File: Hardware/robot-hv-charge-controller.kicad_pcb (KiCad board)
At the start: 2 copper layers, 100 x 100 mm, 136 parts, among them J1 USB2.0_16P, J2 UART_CONN, J3 XT30PW-M, J4 Conn_01x02, J5 XT60PW-M, J6 Conn_01x02, J7 XT60PW-M, J8 Conn_01x03, J9 Conn_01x02, Q2 2SD882, Q3 BC817, Q4 BC817, Q5 2SD882, Q6 2SD882, Q7 MJD41CT4G, SW1 ENABLE, U1 TCAN3414DR, U10 LTV-356T, U11 LTV-356T, U12 LTV-356T, U13 LTV-356T, U14 LTV-356T, U15 CH340C, U2 INA240A1PW, U3 MAX3485, U4 ESP32-WROOM-32E, U5 USBLC6-2SC6, U6 LTV-356T, U7 TLV1117-33, U8 HF116F-80/24-1HTF, U9 LV14340DDAR

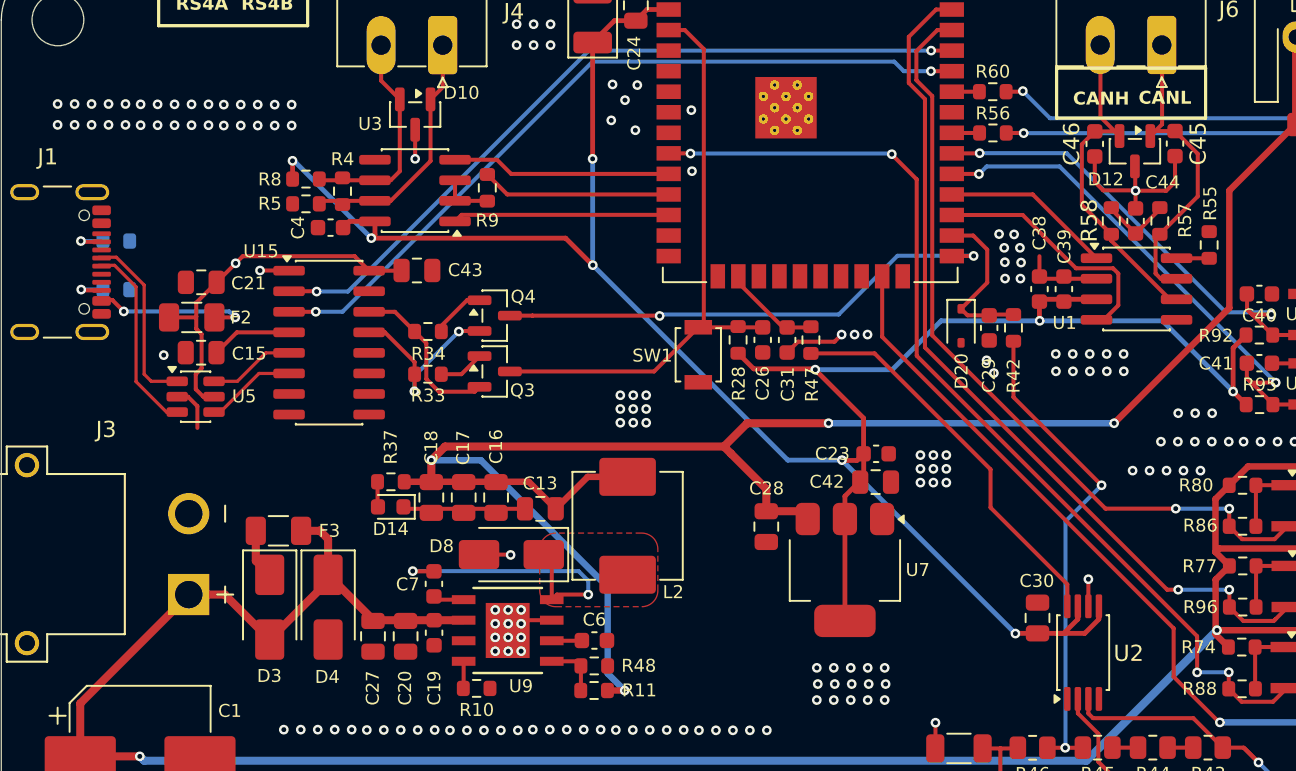
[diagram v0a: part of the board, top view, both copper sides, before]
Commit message: fix(hardware): revise optocoupler control logic
Update relay and communication optocoupler drive networks, then synchronize the related PCB routing and KiCad project metadata.
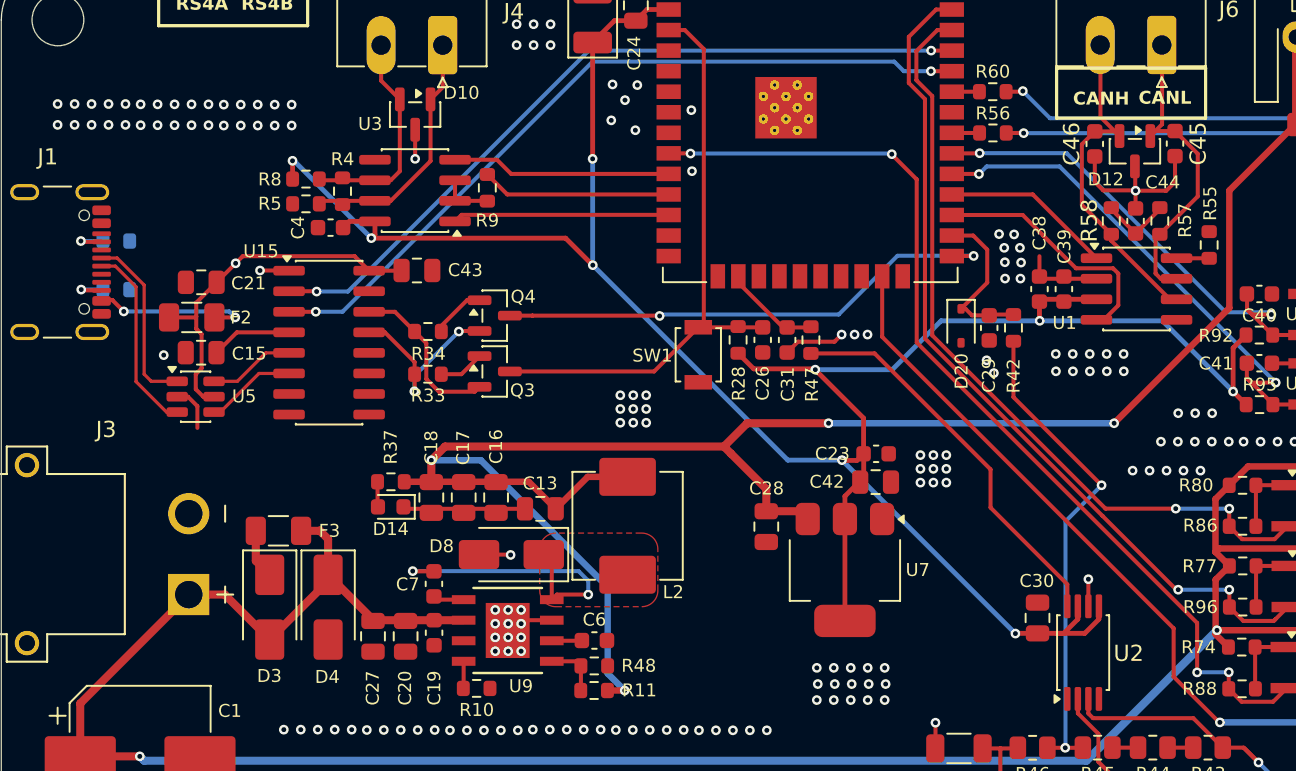
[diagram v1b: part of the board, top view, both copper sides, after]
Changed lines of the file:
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@@
 			(layer "F.Cu"
 				(type "copper")
-				(thickness 0.035)
+				(thickness 0.07)
 			)
 			(layer "dielectric 1"
 				(type "core")
-				(thickness 1.51)
+				(color "FR4 natural")
+				(thickness 1.44)
 				(material "FR4")
 				(epsilon_r 4.5)
@@
 			(layer "B.Cu"
 				(type "copper")
-				(thickness 0.035)
+				(thickness 0.07)
 			)
 			(layer "B.Mask"
@@
 		(capping no)
 		(filling no)
+		(zone_defaults)
 		(pcbplotparams
 			(layerselection 0x00000000_00000000_55555555_55555550)
@@
 	)
 	(segment
+		(start 159.6 51.36)
+		(end 159.32 51.36)
+		(width 0.25)
+		(layer "F.Cu")
+		(net "/Output_Protection_And_Sensing/VOUT_SENSE_ADC")
+	)
+	(segment
 		(start 160.94 49.74)
 		(end 160.94 47.7)
@@
 	(segment
 		(start 161.06 51.7625)
-		(end 159.7225 51.7625)
+		(end 160.0025 51.7625)
 		(width 0.25)
 		(layer "F.Cu")
@@
 	)
 	(segment
-		(start 159.7225 51.7625)
-		(end 159.32 51.36)
+		(start 160.0025 51.7625)
+		(end 159.6 51.36)
 		(width 0.25)
 		(layer "F.Cu")
@@
 	)
 	(segment
-		(start 141.25 41.75)
-		(end 142.59 41.75)
+		(start 156.58 43.36)
+		(end 156.58 53.443884)
 		(width 0.25)
 		(layer "F.Cu")
@@
 	)
 	(segment
-		(start 173.91 71.59)
-		(end 173.91 73.83)
+		(start 141.25 41.75)
+		(end 142.59 41.75)
 		(width 0.25)
 		(layer "F.Cu")
@@
 	)
 	(segment
-		(start 178.6075 75.645)
-		(end 176.665 75.645)
+		(start 173.91 70.773884)
+		(end 173.91 73.83)
 		(width 0.25)
 		(layer "F.Cu")
@@
 	)
 	(segment
-		(start 142.59 41.75)
-		(end 142.6 41.76)
+		(start 155.04 41.82)
+		(end 156.58 43.36)
 		(width 0.25)
 		(layer "F.Cu")
@@
 	)
 	(segment
-		(start 156.58 54.26)
-		(end 173.91 71.59)
+		(start 178.6075 75.645)
+		(end 176.665 75.645)
 		(width 0.25)
 		(layer "F.Cu")
@@
 	)
 	(segment
-		(start 156.58 43.36)
-		(end 156.58 54.26)
+		(start 156.58 53.443884)
+		(end 173.91 70.773884)
 		(width 0.25)
 		(layer "F.Cu")
@@
 	)
 	(segment
-		(start 155.04 41.8)
-		(end 155.04 41.82)
+		(start 142.59 41.75)
+		(end 142.6 41.76)
 		(width 0.25)
 		(layer "F.Cu")
@@
 	)
 	(segment
-		(start 155.04 41.82)
-		(end 156.58 43.36)
+		(start 155.04 41.8)
+		(end 155.04 41.82)
 		(width 0.25)
 		(layer "F.Cu")
@@
 	)
 	(segment
-		(start 108.83 55.4)
-		(end 109.27 55.84)
+		(start 107.16 48.22)
+		(end 108.83 49.89)
 		(width 0.2)
 		(layer "F.Cu")
@@
 	)
 	(segment
-		(start 107.11 48.17)
-		(end 108.83 49.89)
+		(start 108.83 55.4)
+		(end 109.27 55.84)
 		(width 0.2)
 		(layer "F.Cu")
@@
 	)
 	(segment
-		(start 106.02 48.17)
-		(end 107.11 48.17)
+		(start 106.2 48.22)
+		(end 107.16 48.22)
 		(width 0.2)
 		(layer "F.Cu")
@@
 	)
 	(segment
-		(start 107 48.67)
+		(start 107.05 48.72)
 		(end 108.33 50)
 		(width 0.2)
@@
 	)
 	(segment
-		(start 106.02 48.67)
-		(end 107 48.67)
+		(start 110.210001 57.74)
+		(end 110.8725 57.74)
 		(width 0.2)
 		(layer "F.Cu")
@@
 	)
 	(segment
-		(start 110.210001 57.74)
-		(end 110.8725 57.74)
+		(start 106.2 48.72)
+		(end 107.05 48.72)
 		(width 0.2)
 		(layer "F.Cu")
@@
 	)
 	(segment
+		(start 172.74 68.72)
+		(end 172.623604 68.72)
+		(width 0.25)
+		(layer "F.Cu")
+		(net "/Communication_Interfaces/DO2_CMD")
+	)
+	(segment
+		(start 168.066396 64.16)
+		(end 168.063604 64.16)
+		(width 0.25)
+		(layer "F.Cu")
+		(net "/Communication_Interfaces/DO2_CMD")
+	)
+	(segment
 		(start 179.51 69.79)
 		(end 178.71 70.59)
@@
 	)
 	(segment
-		(start 172.74 68.72)
-		(end 172.06 68.72)
+		(start 172.565 68.658604)
+		(end 168.066396 64.16)
 		(width 0.25)
 		(layer "F.Cu")
@@
 	)
 	(segment
-		(start 157.78 32.86)
-		(end 158.75 32.86)
+		(start 172.565 68.661396)
+		(end 172.565 68.658604)
 		(width 0.25)
 		(layer "F.Cu")
@@
 	)
 	(segment
-		(start 156.09 37.396396)
-		(end 156.09 34.55)
+		(start 157.09 53.186396)
+		(end 157.09 38.396396)
 		(width 0.25)
 		(layer "F.Cu")
@@
 	)
 	(segment
-		(start 172.06 68.72)
-		(end 157.09 53.75)
+		(start 172.623604 68.72)
+		(end 172.565 68.661396)
 		(width 0.25)
 		(layer "F.Cu")
@@
 	)
 	(segment
-		(start 157.09 53.75)
-		(end 157.09 38.396396)
+		(start 156.09 37.396396)
+		(end 156.09 34.55)
+		(width 0.25)
+		(layer "F.Cu")
+		(net "/Communication_Interfaces/DO2_CMD")
+	)
+	(segment
+		(start 157.09 38.396396)
+		(end 156.09 37.396396)
 		(width 0.25)
 		(layer "F.Cu")
@@
 	)
 	(segment
-		(start 157.09 38.396396)
-		(end 156.09 37.396396)
+		(start 157.78 32.86)
+		(end 158.75 32.86)
 		(width 0.25)
 		(layer "F.Cu")
@@
 		(width 0.25)
 		(layer "F.Cu")
+		(net "/Communication_Interfaces/DO2_CMD")
+	)
+	(segment
+		(start 168.063604 64.16)
+		(end 157.09 53.186396)
+		(width 0.25)
+		(layer "F.Cu")

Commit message: fix(hardware): reroute PCB for schematic updates
Synchronize PCB routing and net assignments with the revised optocoupler control design, including related auxiliary power and USB signal wiring updates.
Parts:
- removed R86, R88, R96: 10kR, Resistor_SMD:R_0603_1608Metric
- removed R89: 10kR, Resistor_SMD:R_0805_2012Metric
- C2: value 100nF -> 100nF-50V
- C26: value 1uF -> 1uF-50V
- C3: value 100uF -> 100uF-50V
- C44, C45, C46: value 33pF -> 33pF-50V
- F3: value Fuse -> NSMD100
- J3: footprint XT30PW-M:AMASS_XT30PW-M -> RobotChargeController:AMASS_XT30PW-M
- J5, J7: footprint XT60PW-M:AMASS_XT60PW-M -> RobotChargeController:AMASS_XT60PW-M
- R74, R77, R80, R83: value 3.3kR -> 1kR
- U8: footprint HF116F-80-12-24-1HTF:RELAY-TH_HF116F-80-XX-1HTF -> RobotChargeController:RELAY-TH_HF116F-80-XX-1HTF
- U9: footprint LV14340DDAR:SOIC8_DDA_TEX -> RobotChargeController:SOIC8_DDA_TEX
- moved R83 1.05 mm to (179.1, 126.6), turned to 0 degrees
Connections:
- net /Auxiliary_Power_Supply/AUX24_PRE_FUSE renamed Net-(D3-K)
- net /Auxiliary_Power_Supply/BUCK_BOOT renamed Net-(U9-BOOT)
- net /Auxiliary_Power_Supply/BUCK_FB renamed Net-(U9-FB)
- net /Auxiliary_Power_Supply/BUCK_RT_SYNC renamed Net-(U9-RT/SYNC)
- net /Auxiliary_Power_Supply/BUCK_SS renamed Net-(U9-SS)
- net /Auxiliary_Power_Supply/BUCK_SW renamed Net-(D8-K)
- net /Main_Relay_Control/MAIN_RELAY_COIL_N renamed Net-(D7-A)
- net /Output_Protection_And_Sensing/IOUT_SENSE_ADC renamed /MCU_Control/IOUT_SENSE_ADC
- net /Output_Protection_And_Sensing/IOUT_SENSE_RAW renamed Net-(R47-Pad2)
- net /Output_Protection_And_Sensing/VOUT_DIV_RAW renamed Net-(R42-Pad2)
- net /Output_Protection_And_Sensing/VOUT_SENSE_ADC renamed /MCU_Control/VOUT_SENSE_ADC
- C1 pad 1: +24V -> /Auxiliary_Power_Supply/VAUX_IN_P
- C45 pad 2: GND -> Net-(C45-Pad2)
- C46 pad 1: GND -> Net-(C45-Pad2)
- D1 pad 2: DO1_SINK -> DO3_SINK
- D3 pad 2: +24V -> /Auxiliary_Power_Supply/VAUX_IN_P
- D6 pad 2: DO3_SINK -> DO1_SINK
- J3 pad P: +24V -> /Auxiliary_Power_Supply/VAUX_IN_P
- Q2 pad 2: DO1_SINK -> DO3_SINK
- Q6 pad 2: DO3_SINK -> DO1_SINK
- R74 pad 1: +24V -> /Communication_Interfaces/DO1_CMD
- R77 pad 1: +24V -> /Communication_Interfaces/DO2_CMD
- R80 pad 1: +24V -> /Communication_Interfaces/DO3_CMD
- R83 pad 1: +24V -> Net-(R83-Pad1)
- R83 pad 2: Net-(R83-Pad2) -> /MCU_Control/MAIN_RELAY_EN
- U10 pad 2: /Communication_Interfaces/DO3_CMD -> GND
- U11 pad 2: /Communication_Interfaces/DO1_CMD -> GND
- U13 pad 1: Net-(R83-Pad2) -> Net-(R83-Pad1)
- U13 pad 2: /MCU_Control/MAIN_RELAY_EN -> GND
- U5 pad 1: /MCU_Control/USB_CONN_D+ -> /MCU_Control/USB_CONN_D-
- U5 pad 3: /MCU_Control/USB_CONN_D- -> /MCU_Control/USB_CONN_D+
- U5 pad 4: /MCU_Control/USB_D- -> /MCU_Control/USB_D+
- U5 pad 6: /MCU_Control/USB_D+ -> /MCU_Control/USB_D-
- U6 pad 2: /Communication_Interfaces/DO2_CMD -> GND
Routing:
- net +24V: track 333.2 -> 307.7 mm, vias 6 -> 7
- net /Auxiliary_Power_Supply/VAUX_IN_P: track 0.00 -> 21.1 mm
- net /MCU_Control/USB_VBUS_RAW: track 10.2 -> 20.7 mm, vias 2 -> 3
- net GND: track 162.9 -> 173.0 mm, vias 233 -> 234
- net /Communication_Interfaces/DO1_CMD: track 60.9 -> 53.3 mm, vias 4 -> 2
- net Net-(R83-Pad2): track 7.32 -> 0.00 mm
- net /Communication_Interfaces/DO2_CMD: track 53.1 -> 47.1 mm, vias 2 -> 0
- net Net-(R83-Pad1): track 0.00 -> 4.92 mm
- net Net-(J1-CC2): track 2.63 -> 5.49 mm
- net /MCU_Control/USB_CONN_D+: track 11.1 -> 13.6 mm
- net Net-(R74-Pad2): track 4.52 -> 1.96 mm
- net Net-(R77-Pad2): track 4.49 -> 1.95 mm
- net Net-(R80-Pad2): track 4.49 -> 1.96 mm
- net Net-(J1-CC1): track 2.74 -> 5.16 mm
- net /Communication_Interfaces/DO3_CMD: track 48.9 -> 47.4 mm, vias 2 -> 0
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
